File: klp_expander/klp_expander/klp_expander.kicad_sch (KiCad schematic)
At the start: 0 parts

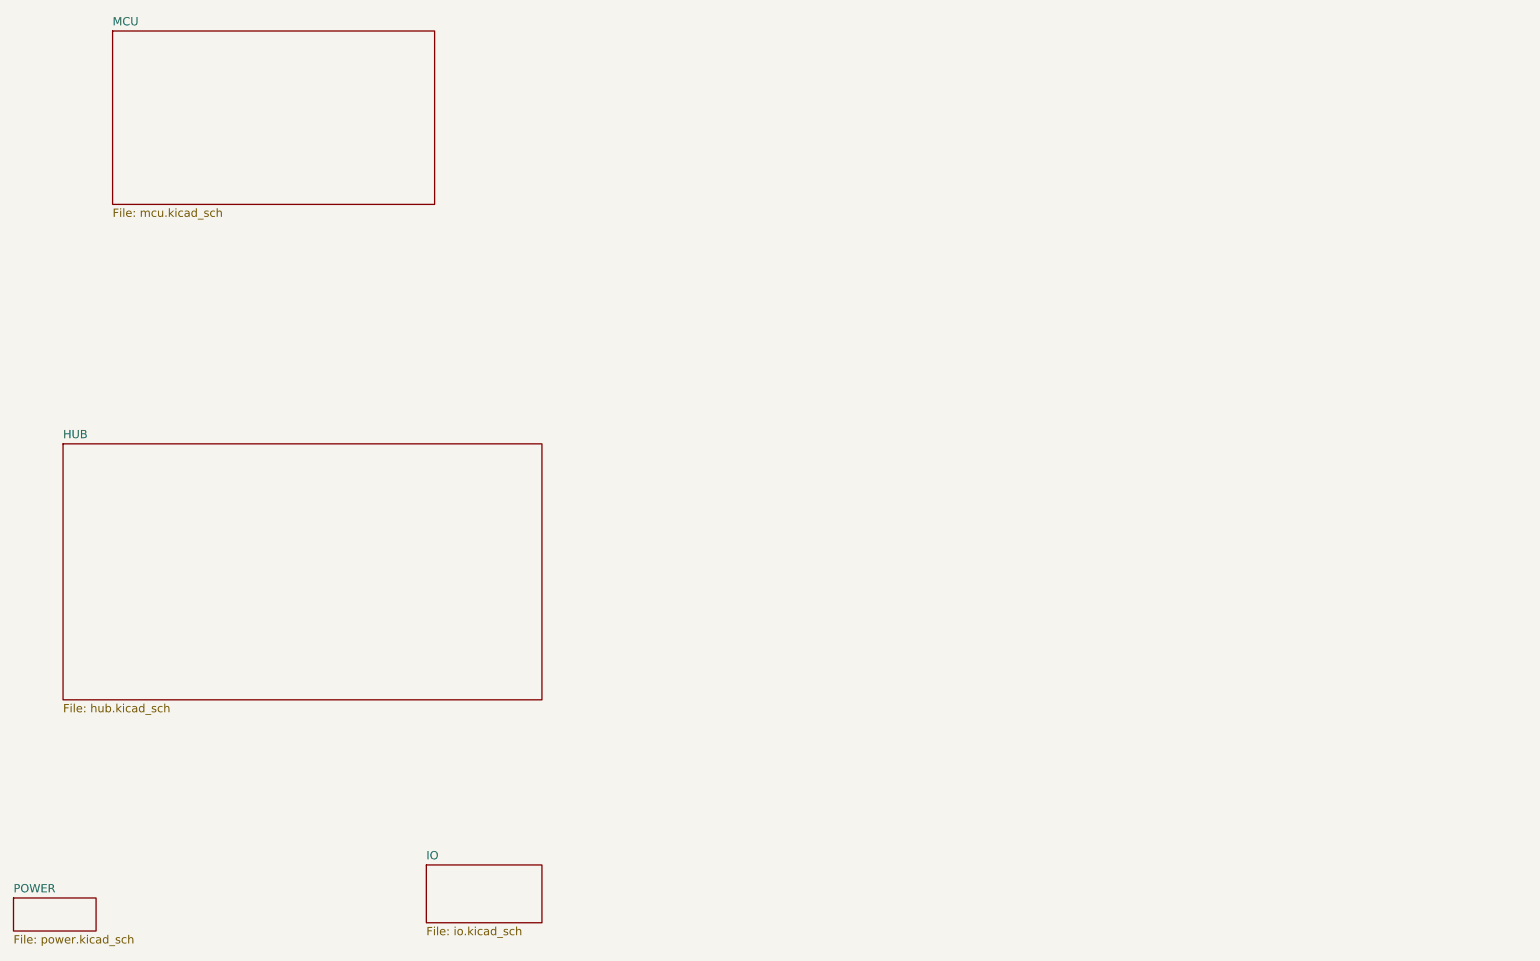
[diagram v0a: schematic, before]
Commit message: feat: merge middle mcu into klp expander. both projects will be merged and will get a new name
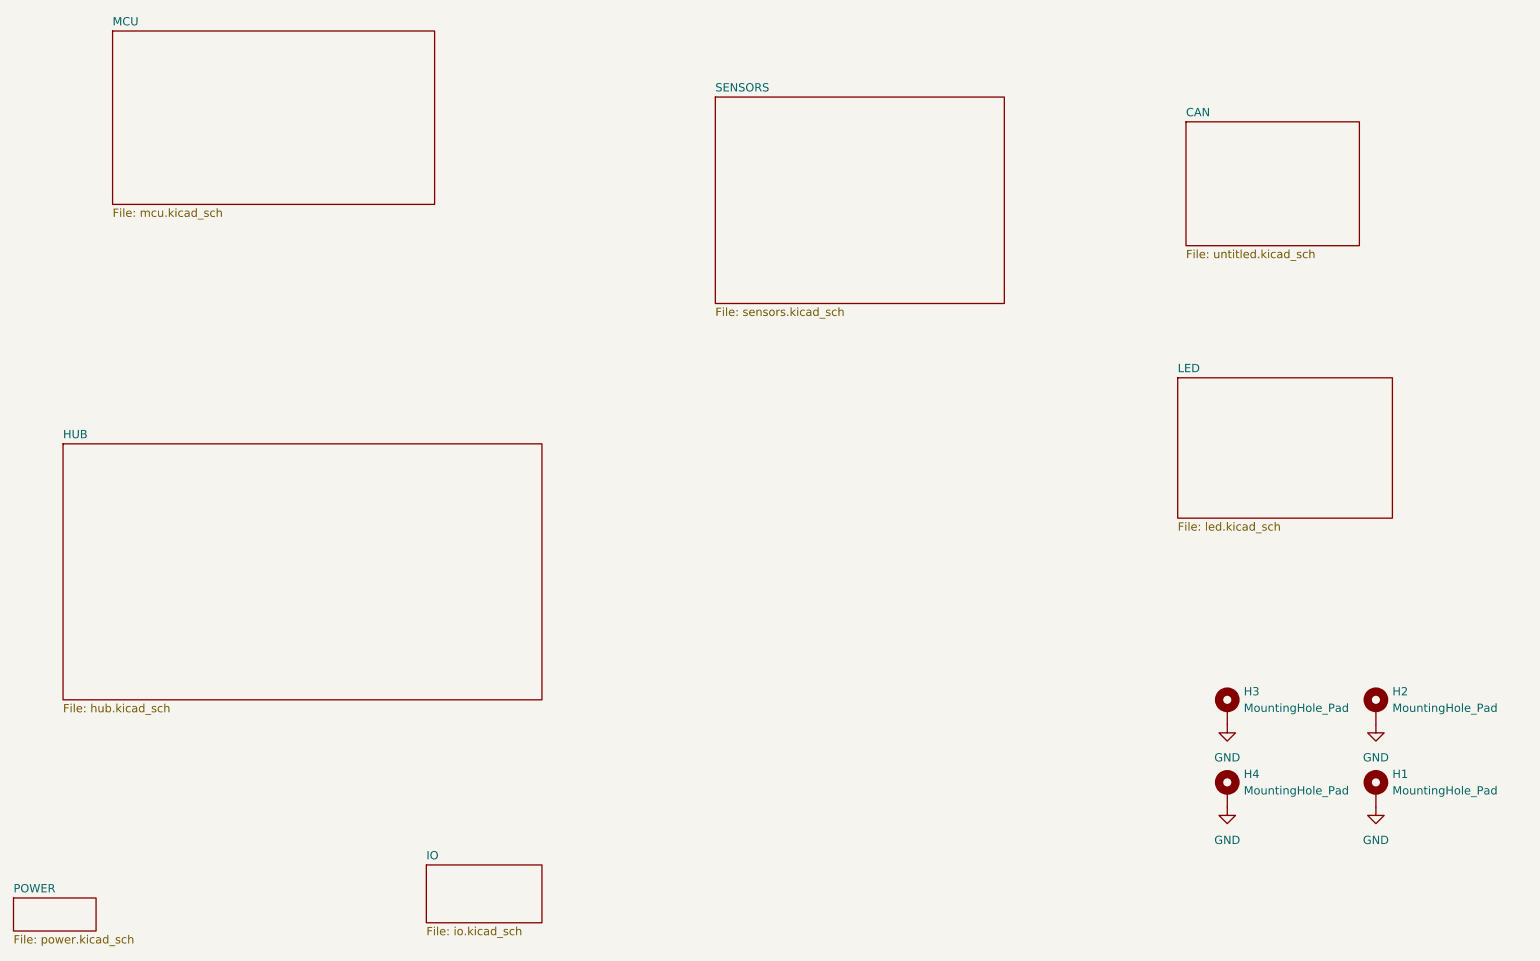
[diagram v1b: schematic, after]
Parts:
- added H1, H2, H3, H4: MountingHole_Pad, MountingHole:MountingHole_3.5mm_Pad, symbol Mechanical:MountingHole_Pad
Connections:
- new net GND: H1.1, H2.1, H3.1, H4.1
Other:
- added sheet CAN (untitled.kicad_sch)
- added sheet LED (led.kicad_sch)
- added sheet SENSORS (sensors.kicad_sch)
